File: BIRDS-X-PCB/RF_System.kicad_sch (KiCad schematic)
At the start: 42 parts, among them J501 60611002111501, U501 SX1276, U502 PE4259, U503 TXKTPCSANF-32

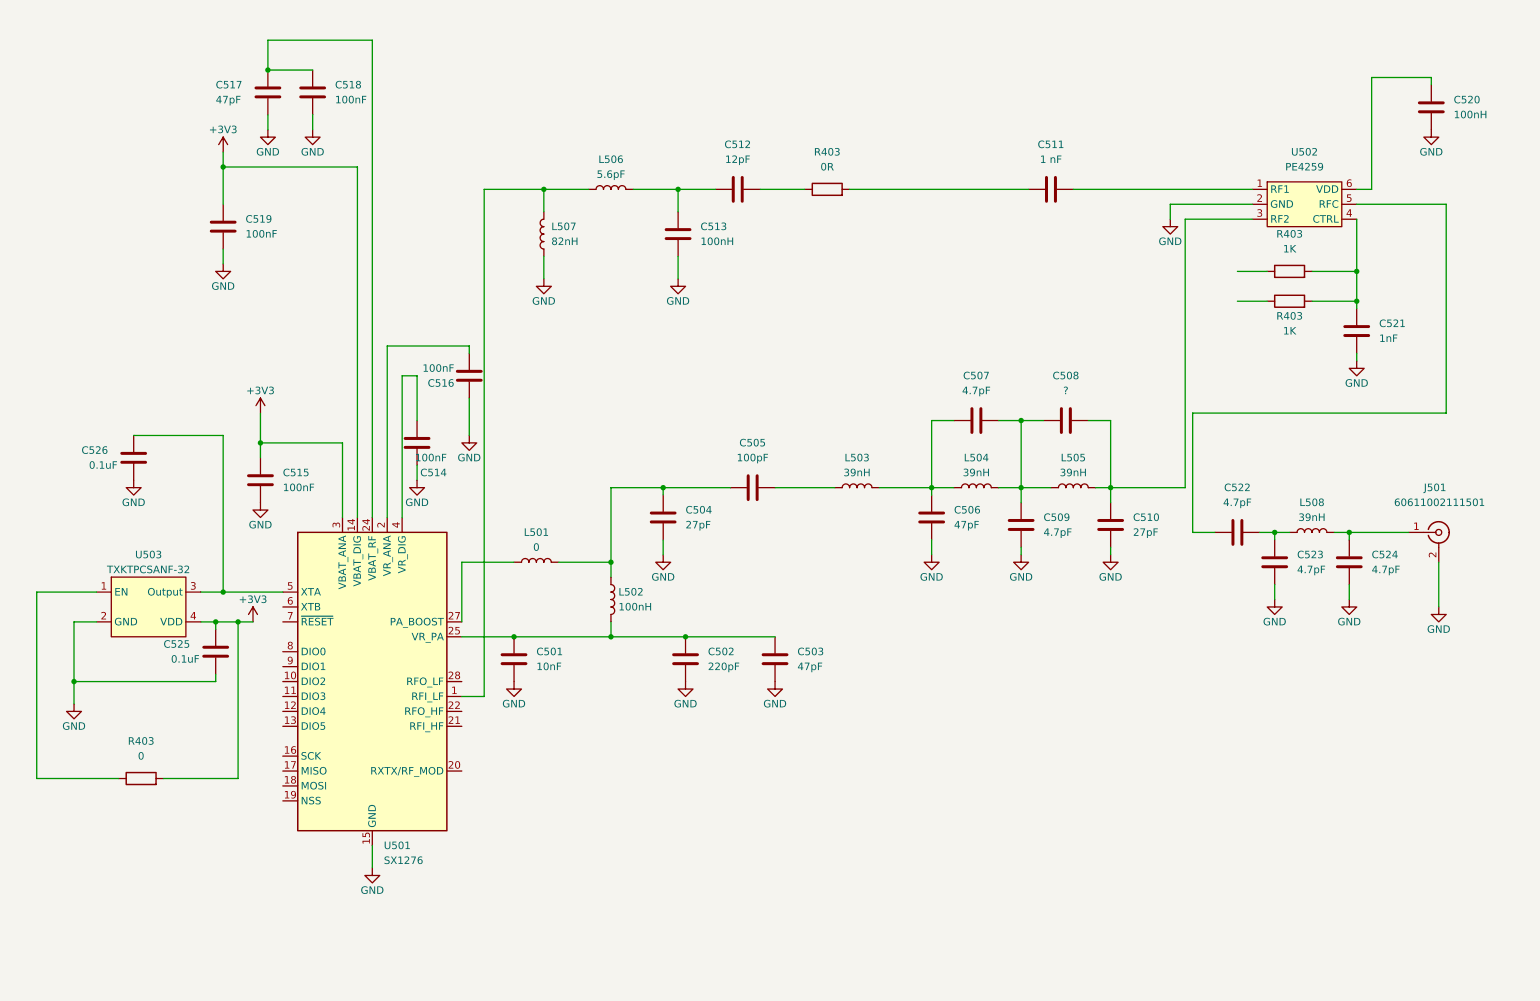
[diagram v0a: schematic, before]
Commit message: Update footprint assignments
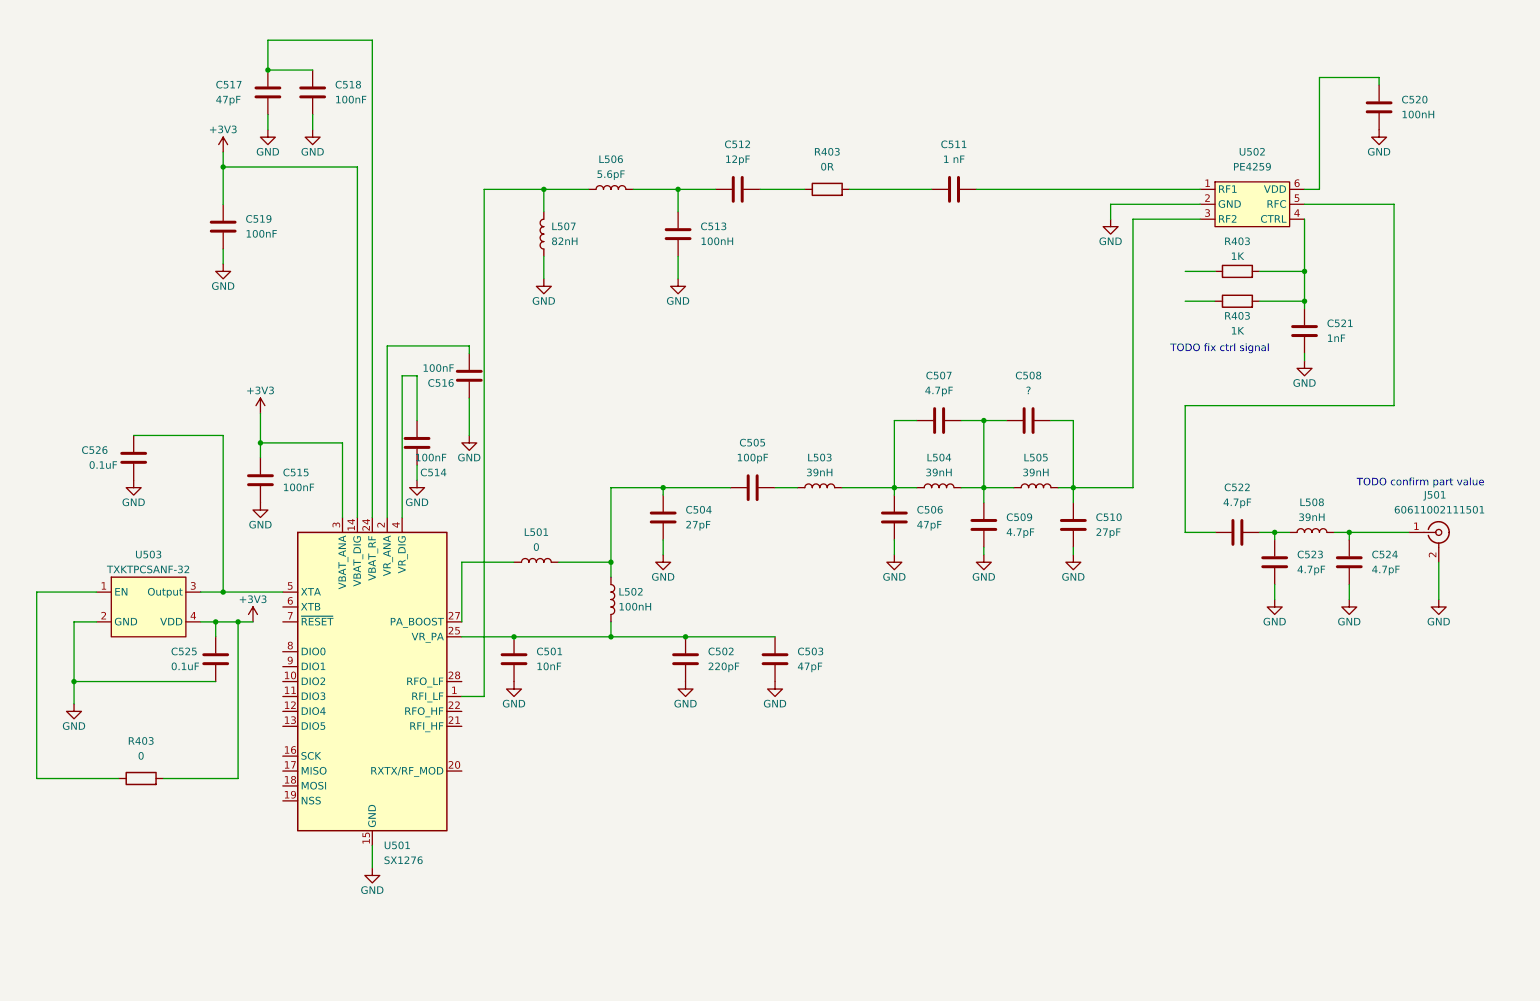
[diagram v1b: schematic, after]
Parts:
- C501, C502, C503, C504, C505, C506, C507, C508, C509, C510, C511, C512, C513, C514, C515, C516, C517, C518, C519, C520, C521, C522, C523, C524, C525, C526: footprint (none) -> Capacitor_SMD:C_0805_2012Metric_Pad1.18x1.45mm_HandSolder
- J501: footprint (none) -> Connector_Coaxial:SMA_Amphenol_901-143_Horizontal
- L501, L502, L503, L504, L505, L506, L507, L508: footprint (none) -> Inductor_SMD:L_0603_1608Metric_Pad1.05x0.95mm_HandSolder
- U503: footprint (none) -> Crystal:Crystal_SMD_3225-4Pin_3.2x2.5mm
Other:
- note added: "TODO confirm part value"
- note added: "TODO fix ctrl signal"
- moved on the sheet: C506, C507, C508, C509, C510, C511, C520, C521, C525, L503, L504, L505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

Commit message: Update footprints to 0603
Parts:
- C501, C502, C503, C504, C505, C506, C507, C508, C509, C510, C511, C512, C513, C514, C515, C516, C517, C518, C519, C520, C521, C522, C523, C524, C525, C526: footprint Capacitor_SMD:C_0805_2012Metric_Pad1.18x1.45mm_HandSolder -> Capacitor_SMD:C_0603_1608Metric_Pad1.08x0.95mm_HandSolder
- R403: footprint Resistor_SMD:R_0805_2012Metric_Pad1.20x1.40mm_HandSolder -> Resistor_SMD:R_0603_1608Metric_Pad0.98x0.95mm_HandSolder

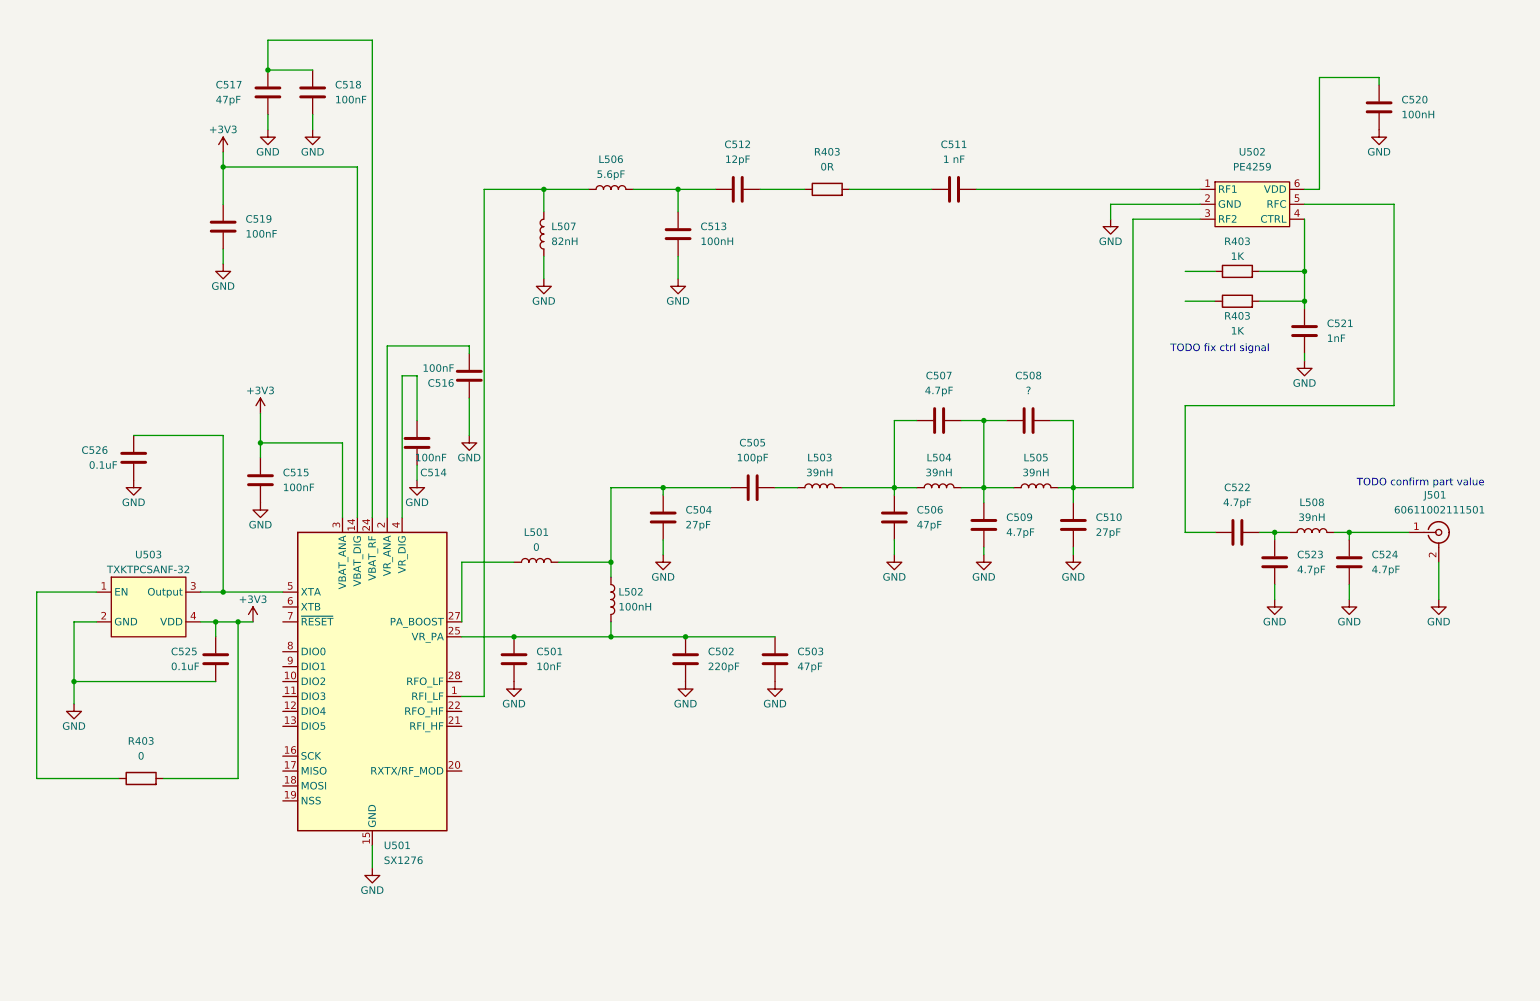
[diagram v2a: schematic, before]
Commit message: Do major layout
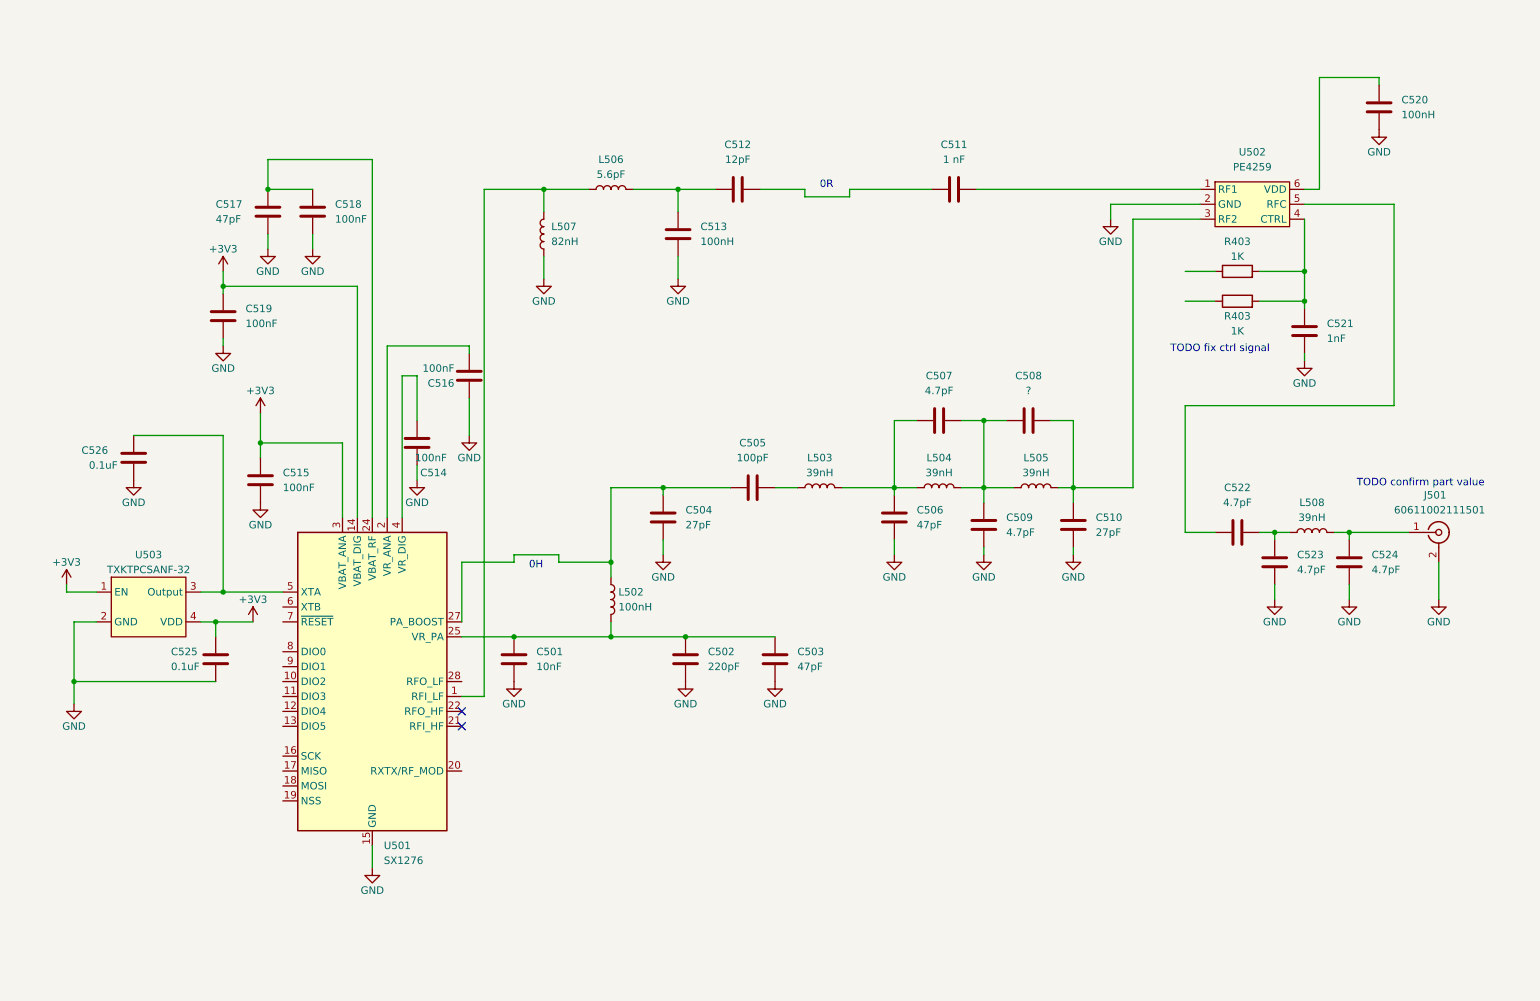
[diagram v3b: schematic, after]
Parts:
- removed L501: 0, Inductor_SMD:L_0603_1608Metric_Pad1.05x0.95mm_HandSolder, symbol Device:L
- removed R403: 0, Resistor_SMD:R_0603_1608Metric_Pad0.98x0.95mm_HandSolder, symbol Device:R
- removed R403: 0R, Resistor_SMD:R_0603_1608Metric_Pad0.98x0.95mm_HandSolder, symbol Device:R
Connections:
- net +3V3: now also U503.1 (EN)
- net at U501.27 (PA_BOOST): now also C504.1, C505.1, L502.1
- net at C512.2: now also C511.1
- no-connect marks 0 -> 2
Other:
- note added: "0H"
- note added: "0R"
- moved on the sheet: C517, C518, C519
